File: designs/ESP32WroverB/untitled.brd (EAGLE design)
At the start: 31 x 47.5 mm, 19 parts, among them IC6 ESP32-WROVER-B

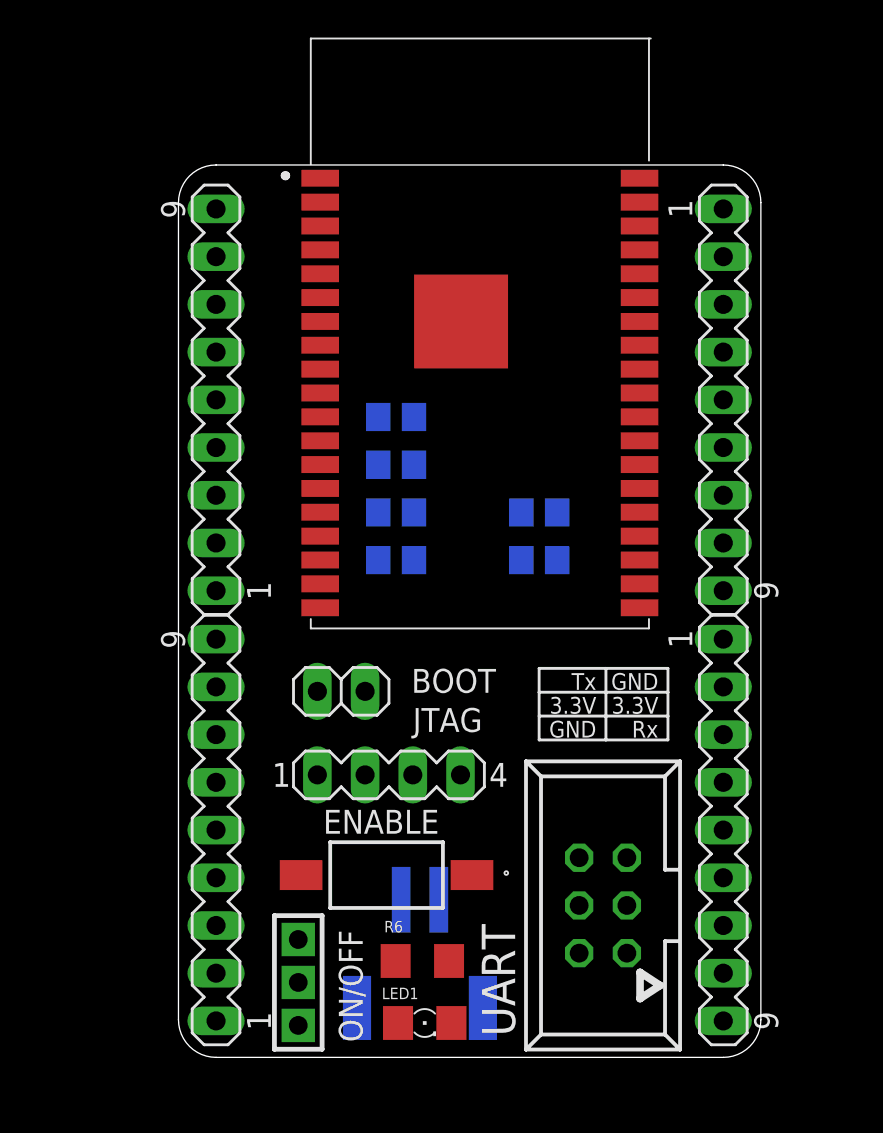
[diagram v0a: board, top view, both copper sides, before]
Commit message: added design block Logo
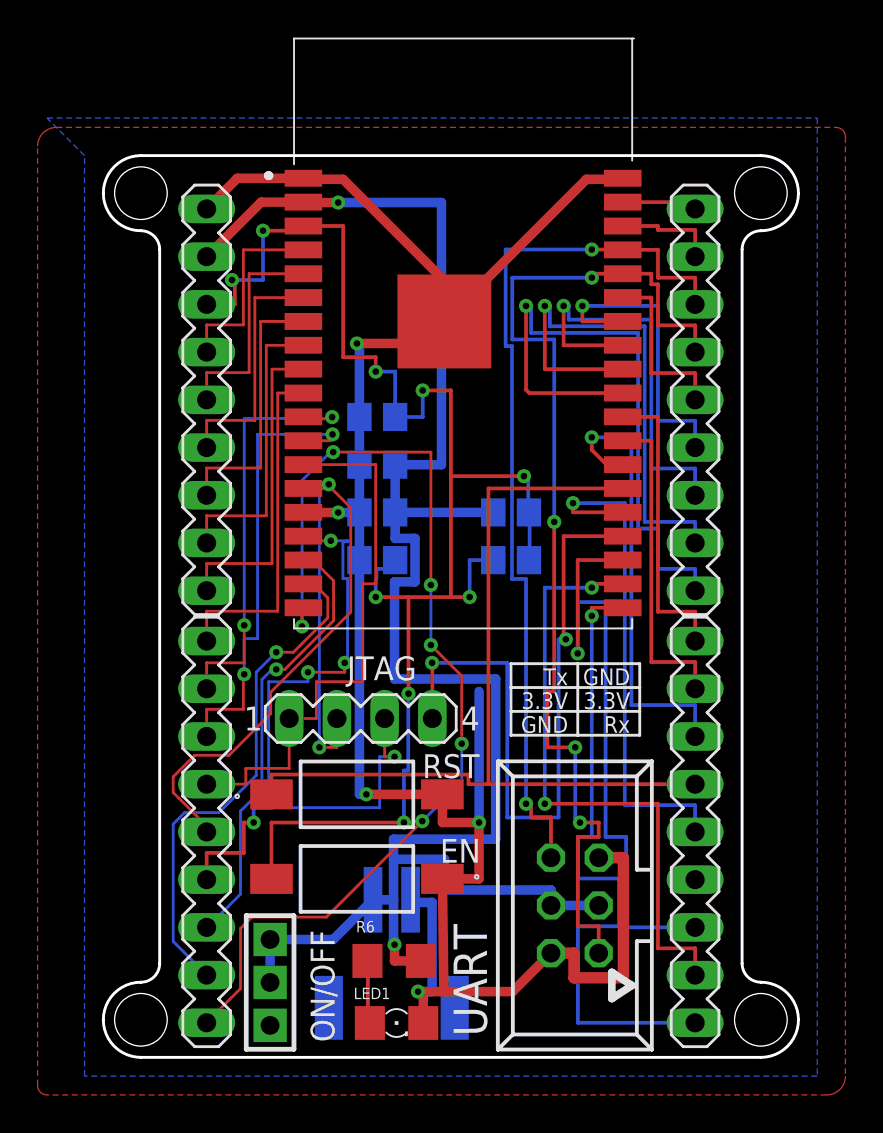
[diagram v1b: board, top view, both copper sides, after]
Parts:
- removed BOOT: (no value), CommonParts:1X02
- removed ENABLE: FSMSMTR, FSMSMTR:FSMSM
- removed SV3, SV4: (no value), con-lstb:MA09-1
- added EN, RST: FSMSMTR, FSMSMTR:FSMSM
- added SV5, SV6: (no value), CommonParts:MA09-1
- SV1, SV2: device con-lstb:MA09-1 -> CommonParts:MA09-1
- moved SV1 34.3 mm to (29.5, 12.0), turned to 270 degrees
- moved SV2 34.3 mm to (29.5, 35.0), turned to 270 degrees
- moved JTAG 3.35 mm to (11.7, 18.0)
- moved LED1 1.50 mm to (13.6, 1.83)
- moved POWER 1.50 mm to (13.4, 8.39)
- moved R1 1.50 mm to (19.7, 29.0)
- moved R2 1.50 mm to (19.7, 26.5)
- moved R6 1.50 mm to (13.5, 5.13)
- moved UART 1.50 mm to (23.1, 8.09)
- moved ON/OFF 1.50 mm to (6.62, 3.48)
- moved C1 1.00 mm to (12.6, 34.1)
- moved C2 1.00 mm to (12.6, 31.5)
- moved C3 1.00 mm to (12.6, 29.0)
- moved C4 1.00 mm to (12.6, 26.5)
- moved IC6 0.89 mm to (16.5, 38.5)
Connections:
- net 3.3V: now also SV5.8; no longer ON/OFF.P$3, SV1.8
- net CLK: now also SV1.9; no longer SV3.9
- net CMD: now also SV6.1; no longer SV2.1
- net EN: now also EN.2, SV5.7; no longer ENABLE.2, SV1.7
- net GND: now also EN.1, RST.2, SV5.9; no longer BOOT.2, ENABLE.1, SV1.9
- net GPIO12: now also SV6.5; no longer SV2.5
- net GPIO13: now also SV6.4; no longer SV2.4
- net GPIO14: now also SV6.6; no longer SV2.6
- net IO0: now also RST.1, SV1.4; no longer BOOT.1, SV3.4
- net IO15: now also SV1.6; no longer SV3.6
- net IO18: now also SV2.8; no longer SV4.8
- net IO19: now also SV2.7; no longer SV4.7
- net IO2: now also SV1.5; no longer SV3.5
- net IO21: now also SV2.5; no longer SV4.5
- net IO22: now also SV2.2; no longer SV4.2
- net IO23: now also SV2.1; no longer SV4.1
- net IO25: now also SV6.9; no longer SV2.9
- net IO26: now also SV6.8; no longer SV2.8
- net IO27: now also SV6.7; no longer SV2.7
- net IO32: now also SV5.2; no longer SV1.2
- net IO33: now also SV5.1; no longer SV1.1
- net IO34: now also SV5.4; no longer SV1.4
- net IO35: now also SV5.3; no longer SV1.3
- net IO4: now also SV1.3; no longer SV3.3
- net IO5: now also SV2.9; no longer SV4.9
- net NC_1: now also SV1.2; no longer SV3.2
- net NC_2: now also SV1.1; no longer SV3.1
- net NC_3: now also SV2.6; no longer SV4.6
- net RXD0: now also SV2.4; no longer SV4.4
- net SD0: now also SV1.8; no longer SV3.8
- net SD1: now also SV1.7; no longer SV3.7
- net SD2: now also SV6.3; no longer SV2.3
- net SD3: now also SV6.2; no longer SV2.2
- net SEN_VN: now also SV5.5; no longer SV1.5
- net SEN_VP: now also SV5.6; no longer SV1.6
- net TXD0: now also SV2.3; no longer SV4.3
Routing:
- net GND: track 0.00 -> 118.8 mm, vias 0 -> 5
- net 3.3V: track 0.00 -> 99.3 mm, vias 0 -> 2
- net EN: track 0.00 -> 82.9 mm, vias 0 -> 9
- net RXD0: track 0.00 -> 57.6 mm, vias 0 -> 4
- net CMD: track 0.00 -> 55.5 mm, vias 0 -> 6
- net TXD0: track 0.00 -> 47.8 mm, vias 0 -> 2
- net IO0: track 0.00 -> 47.0 mm
- net GPIO12: track 0.00 -> 43.2 mm, vias 0 -> 2
- net GPIO13: track 0.00 -> 40.8 mm, vias 0 -> 5
- net GPIO15: track 0.00 -> 36.6 mm, vias 0 -> 2
- net CLK: track 0.00 -> 35.2 mm, vias 0 -> 1
- net IO5: track 0.00 -> 33.8 mm, vias 0 -> 1
- net SD1: track 0.00 -> 33.7 mm, vias 0 -> 1
- net SD0: track 0.00 -> 33.0 mm, vias 0 -> 2
- net GPIO14: track 0.00 -> 29.9 mm
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- added copper zone on layer 1, net GND
- added copper zone on layer 16, net GND
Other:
- board size 31 x 47.5 mm -> 37 x 48 mm
- board text added: "GPIO12"
- board text added: "GPIO13"
- board text added: "GPIO14"
- board text added: "GPIO15"

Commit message: finished mainboard
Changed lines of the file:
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@@
 <?xml version="1.0" encoding="utf-8"?>
 <!DOCTYPE eagle SYSTEM "eagle.dtd">
-<eagle version="9.4.2">
+<eagle version="9.5.1">
 <drawing>
 <settings>
@@
 <setting verticaltext="up"/>
 </settings>
-<grid distance="0.25" unitdist="mm" unit="mm" style="lines" multiple="10" display="yes" altdistance="5" altunitdist="mil" altunit="mil"/>
+<grid distance="1" unitdist="mm" unit="mm" style="lines" multiple="1" display="yes" altdistance="5" altunitdist="mil" altunit="mil"/>
 <layers>
 <layer number="1" name="Top" color="4" fill="1" visible="yes" active="yes"/>
@@
 <wire x1="8.882" y1="46.7868" x2="8.65" y2="46.792" width="0.1524" layer="1"/>
 <polygon width="0.1524" layer="1">
-<vertex x="-4.5" y="49.5"/>
-<vertex x="37" y="49.5" curve="-90"/>
-<vertex x="37.5" y="49"/>
-<vertex x="37.5" y="-1" curve="-90"/>
-<vertex x="36.5" y="-2"/>
-<vertex x="-5" y="-2" curve="-90"/>
-<vertex x="-5.5" y="-1.5"/>
-<vertex x="-5.5" y="48.5" curve="-90"/>
+<vertex x="-2" y="48"/>
+<vertex x="-2" y="0"/>
+<vertex x="35" y="0"/>
+<vertex x="35" y="48"/>
 </polygon>
-<polygon width="0.01" layer="16">
-<vertex x="-5" y="50"/>
-<vertex x="36" y="50"/>
-<vertex x="36" y="-1"/>
-<vertex x="-3" y="-1"/>
-<vertex x="-3" y="48"/>
+<polygon width="0.1524" layer="16">
+<vertex x="-2" y="48"/>
+<vertex x="-2" y="0"/>
+<vertex x="35" y="0"/>
+<vertex x="35" y="48"/>
 </polygon>
 </signal>

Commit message: added last design tunes
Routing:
- net GND: track 118.8 -> 120.2 mm
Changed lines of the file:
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@@
 <setting verticaltext="up"/>
 </settings>
-<grid distance="1" unitdist="mm" unit="mm" style="lines" multiple="1" display="yes" altdistance="5" altunitdist="mil" altunit="mil"/>
+<grid distance="0.1" unitdist="mm" unit="mm" style="lines" multiple="1" display="yes" altdistance="5" altunitdist="mil" altunit="mil"/>
 <layers>
 <layer number="1" name="Top" color="4" fill="1" visible="yes" active="yes"/>
@@
 <layer number="27" name="tValues" color="7" fill="1" visible="yes" active="yes"/>
 <layer number="28" name="bValues" color="7" fill="1" visible="yes" active="yes"/>
-<layer number="29" name="tStop" color="7" fill="3" visible="no" active="yes"/>
-<layer number="30" name="bStop" color="7" fill="6" visible="no" active="yes"/>
+<layer number="29" name="tStop" color="7" fill="3" visible="yes" active="yes"/>
+<layer number="30" name="bStop" color="7" fill="6" visible="yes" active="yes"/>
 <layer number="31" name="tCream" color="7" fill="4" visible="no" active="yes"/>
 <layer number="32" name="bCream" color="7" fill="5" visible="no" active="yes"/>
@@
 <contactref element="IC6" pad="15"/>
 <contactref element="IC6" pad="38"/>
-<contactref element="IC6" pad="39"/>
 <contactref element="IC6" pad="1"/>
 <contactref element="EN" pad="1"/>
@@
 <wire x1="14.75" y1="3.5" x2="15.03" y2="3.22" width="0.508" layer="1"/>
 <wire x1="15.03" y1="3.22" x2="15.03" y2="1.829" width="0.508" layer="1"/>
-<wire x1="14.75" y1="3.5" x2="16.126" y2="3.5" width="0.508" layer="1"/>
-<wire x1="16.126" y1="3.5" x2="19.781" y2="3.5" width="0.508" layer="1"/>
+<wire x1="14.75" y1="3.5" x2="16.226" y2="3.5" width="0.508" layer="1"/>
+<wire x1="16.226" y1="3.5" x2="19.781" y2="3.5" width="0.508" layer="1"/>
 <wire x1="19.781" y1="3.5" x2="21.828" y2="5.547" width="0.508" layer="1"/>
-<wire x1="16.15" y1="39.172" x2="23.716" y2="46.738" width="0.508" layer="1"/>
-<wire x1="23.716" y1="46.738" x2="25.646" y2="46.738" width="0.508" layer="1"/>
+<wire x1="23.716" y1="46.738" x2="24" y2="46.738" width="0.508" layer="1"/>
+<wire x1="24" y1="46.738" x2="25.646" y2="46.738" width="0.508" layer="1"/>
 <wire x1="25.646" y1="46.738" x2="25.65" y2="46.738" width="0.508" layer="1"/>
-<wire x1="16.15" y1="39.172" x2="16.15" y2="41.35" width="0.508" layer="1"/>
 <wire x1="16.15" y1="41.35" x2="10.762" y2="46.738" width="0.508" layer="1"/>
 <wire x1="10.762" y1="46.738" x2="8.882" y2="46.738" width="0.508" layer="1"/>
@@
 <wire x1="8.65" y1="46.792" x2="5.132" y2="46.792" width="0.508" layer="1"/>
 <wire x1="5.132" y1="46.792" x2="3.5" y2="45.16" width="0.508" layer="1"/>
-<wire x1="16.15" y1="39.172" x2="16.15" y2="38" width="0.508" layer="1"/>
 <wire x1="16.15" y1="38" x2="11.5" y2="38" width="0.508" layer="1"/>
 <via x="11.5" y="38" extent="1-16" drill="0.35"/>
@@
 <wire x1="11.634" y1="29.007" x2="11.634" y2="26.467" width="0.508" layer="16"/>
 <wire x1="11.634" y1="29.007" x2="11.634" y2="29" width="0.508" layer="16"/>
-<wire x1="11.634" y1="29" x2="10.5" y2="29" width="0.508" layer="16"/>
-<via x="10.5" y="29" extent="1-16" drill="0.35"/>
-<wire x1="10.5" y1="29" x2="8.65" y2="29" width="0.508" layer="1"/>
+<wire x1="11.634" y1="29" x2="10.3" y2="29" width="0.508" layer="16"/>
+<via x="10.3" y="29" extent="1-16" drill="0.35"/>
+<wire x1="10.3" y1="29" x2="8.65" y2="29" width="0.508" layer="1"/>
 <wire x1="8.65" y1="29" x2="8.65" y2="29.012" width="0.508" layer="1"/>
 <wire x1="11.634" y1="34.087" x2="11.634" y2="38" width="0.508" layer="16"/>
@@
 <wire x1="18" y1="19.482" x2="18" y2="12.5" width="0.508" layer="16"/>
 <via x="18" y="12.5" extent="1-16" drill="0.35"/>
-<wire x1="16.05" y1="9.5" x2="16.126" y2="3.5" width="0.508" layer="1"/>
+<wire x1="16.05" y1="9.5" x2="16.151284375" y2="9.398715625" width="0.508" layer="1"/>
+<wire x1="16.226" y1="3.5" x2="16.151284375" y2="9.398715625" width="0.508" layer="1"/>
 <contactref element="RST" pad="2"/>
 <wire x1="16.05" y1="9.5" x2="18" y2="9.5" width="0.508" layer="1"/>
@@
 <vertex x="35" y="48"/>
 </polygon>
+<contactref element="IC6" pad="39"/>
+<wire x1="24" y1="46.738" x2="23.938" y2="46.8" width="0.508" layer="1"/>
+<wire x1="23.938" y1="46.8" x2="16.15" y2="46.8" width="0.508" layer="1"/>
+<wire x1="16.15" y1="46.8" x2="16.15" y2="39.172" width="0.508" layer="1"/>
 </signal>
 <signal name="3.3V">
@@
 <wire x1="23.25" y1="16.5" x2="23.1194" y2="16.5" width="0.2" layer="16"/>
 <via x="23.1194" y="16.5" extent="1-16" drill="0.35"/>
-<wire x1="21.6372" y1="19.4822" x2="22" y2="19.4822" width="0.2" layer="1"/>
-<wire x1="22" y1="19.4822" x2="22" y2="28.5" width="0.2" layer="1"/>
+<wire x1="21.6372" y1="19.4822" x2="21.9" y2="19.4822" width="0.2" layer="1"/>
+<wire x1="21.9" y1="28.4" x2="21.9" y2="19.4822" width="0.2" layer="1"/>
+<wire x1="21.9" y1="28.4" x2="22" y2="28.5" width="0.2" layer="1"/>
 <wire x1="23.1194" y1="16.5" x2="21.6372" y2="16.5" width="0.2" layer="1"/>
 <wire x1="21.6372" y1="16.5" x2="21.6372" y2="19.4822" width="0.2" layer="1"/>
@@
 <via x="9.5" y="16.5" extent="1-16" drill="0.35"/>
 <wire x1="9.5" y1="16.5" x2="9.5" y2="30.5" width="0.1524" layer="16"/>
-<wire x1="9.5" y1="30.5" x2="10" y2="30.5" width="0.1524" layer="16"/>
-<via x="10" y="30.5" extent="1-16" drill="0.35"/>
-<wire x1="10" y1="30.5" x2="10" y2="30.282" width="0.1524" layer="1"/>
-<wire x1="10" y1="30.282" x2="8.65" y2="30.282" width="0.1524" layer="1"/>
+<wire x1="9.5" y1="30.5" x2="10.3" y2="30.5" width="0.1524" layer="16"/>
+<via x="10.3" y="30.5" extent="1-16" drill="0.35"/>
+<wire x1="10.3" y1="30.5" x2="10.3" y2="30.282" width="0.1524" layer="1"/>
+<wire x1="10.3" y1="30.282" x2="8.65" y2="30.282" width="0.1524" layer="1"/>
 <wire x1="3.4718" y1="12.3444" x2="3.4718" y2="12.0396" width="0.1524" layer="1"/>
 <wire x1="1.7192" y1="14.097" x2="3.4718" y2="12.3444" width="0.1524" layer="1"/>
@@
 <wire x1="11.168" y1="23.6982" x2="6.9008" y2="19.431" width="0.1524" layer="1"/>
 <wire x1="11.168" y1="29.2608" x2="11.168" y2="23.6982" width="0.1524" layer="1"/>
-<wire x1="10.025" y1="30.4038" x2="11.168" y2="29.2608" width="0.1524" layer="1"/>
+<wire x1="10.4303375" y1="29.9984625" x2="11.168" y2="29.2608" width="0.1524" layer="1"/>
 <wire x1="3.4718" y1="12.0396" x2="3.5" y2="12" width="0.1524" layer="1"/>
-<wire x1="10.025" y1="30.4038" x2="10" y2="30.5" width="0.1524" layer="1"/>
+<wire x1="10.4303375" y1="29.9984625" x2="10.3" y2="30.5" width="0.1524" layer="1"/>
 </signal>
 <signal name="GPIO13">
@@
 <contactref element="SV6" pad="4"/>
 <wire x1="8.65" y1="27.742" x2="8.65" y2="27.5" width="0.1524" layer="1"/>
-<wire x1="8.65" y1="27.5" x2="10.1068" y2="27.5" width="0.1524" layer="1"/>
-<via x="10.1068" y="27.5" extent="1-16" drill="0.35"/>
-<wire x1="10.1068" y1="27.5" x2="11" y2="27.5" width="0.1524" layer="16"/>
+<wire x1="8.65" y1="27.5" x2="10.4068" y2="27.5" width="0.1524" layer="1"/>
+<via x="10.4068" y="27.5" extent="1-16" drill="0.35"/>
+<wire x1="10.4068" y1="27.5" x2="11" y2="27.5" width="0.1524" layer="16"/>
 <wire x1="11" y1="27.5" x2="11" y2="27.4456" width="0.1524" layer="16"/>
 <wire x1="11" y1="27.4456" x2="10.7554" y2="27.4456" width="0.1524" layer="16"/>
@@
 <contactref element="IC6" pad="23"/>
 <wire x1="25.65" y1="27.742" x2="22.5" y2="27.742" width="0.2" layer="1"/>
-<wire x1="22.5" y1="27.742" x2="22.5" y2="22.25" width="0.2" layer="1"/>
-<wire x1="22.5" y1="22.25" x2="22.6194" y2="22.25" width="0.2" layer="1"/>
-<via x="22.6194" y="22.25" extent="1-16" drill="0.35"/>
-<wire x1="22.6194" y1="22.25" x2="22.2322" y2="22.25" width="0.2" layer="16"/>
-<wire x1="22.2322" y1="22.25" x2="22.2322" y2="12.7678" width="0.2" layer="16"/>
+<wire x1="22.5" y1="27.742" x2="22.5" y2="22.75" width="0.2" layer="1"/>
+<wire x1="22.5" y1="22.75" x2="22.6194" y2="22.75" width="0.2" layer="1"/>
+<via x="22.6194" y="22.75" extent="1-16" drill="0.35"/>
+<wire x1="22.6194" y1="22.75" x2="22.2322" y2="22.75" width="0.2" layer="16"/>
+<wire x1="22.2322" y1="22.75" x2="22.2322" y2="12.7678" width="0.2" layer="16"/>
 <wire x1="22.2322" y1="12.7678" x2="19.5" y2="12.7678" width="0.2" layer="16"/>
 <wire x1="19.5" y1="12.7678" x2="19.5" y2="21" width="0.2" layer="16"/>
@@
 <via x="24" y="33" extent="1-16" drill="0.35"/>
 <wire x1="24" y1="33" x2="26.1108" y2="33" width="0.2" layer="16"/>
-<wire x1="29.5" y1="18.754" x2="29.5" y2="17.08" width="0.2" layer="16"/>
-<wire x1="26.1108" y1="33" x2="26.1108" y2="18.754" width="0.2" layer="16"/>
-<wire x1="26.1108" y1="18.754" x2="29.5" y2="18.754" width="0.2" layer="16"/>
+<wire x1="29.5" y1="18.554" x2="29.5" y2="17.08" width="0.2" layer="16"/>
+<wire x1="26.1108" y1="33" x2="26.1108" y2="18.554" width="0.2" layer="16"/>
+<wire x1="26.1108" y1="18.554" x2="29.5" y2="18.554" width="0.2" layer="16"/>
 </signal>
 <signal name="NC_1">
